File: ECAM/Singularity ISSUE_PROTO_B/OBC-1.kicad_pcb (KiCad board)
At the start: 6 copper layers, 42.8 x 42.8 mm, 111 parts, among them J1 ERM8-020-X, J2 ERF6-020-X, J3 Conn_01x02_Female, Q1 MGSF1N02L, Q2 MGSF1N02L, U1 TPS62850x-Q1, U10 FM33256B, U11 TMS5701227CZWTQQ1, U2 TPS62850x-Q1, U3 LTC4353, U4 SN65HVD230M-EP, U5 SN65HVD230M-EP, U6 SN65HVD230M-EP, U7 CY15B108QI, U8 S70FL01GS, X1 ASTMTXK-32.768KHZ, X2 LFTCXO075797

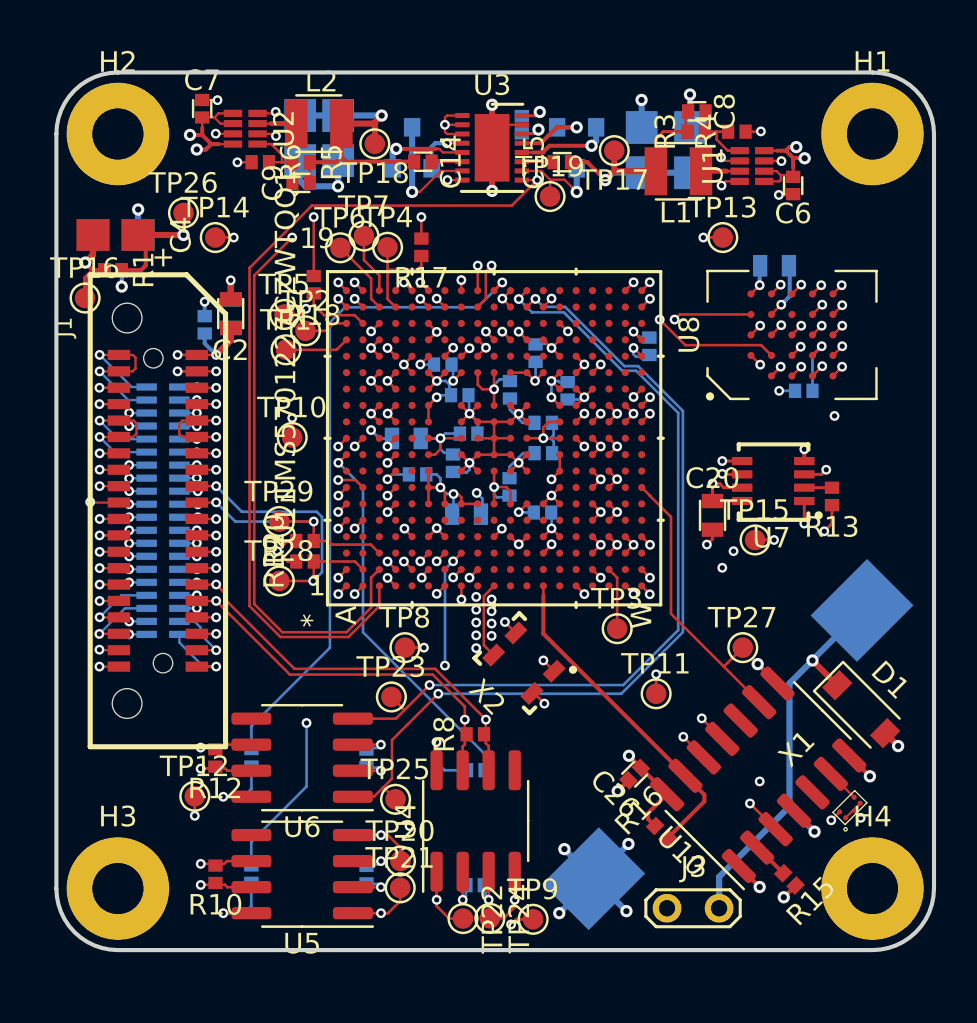
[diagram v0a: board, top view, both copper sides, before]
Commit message: updated PCB layout for Issue B supervisor/RTC circuitry
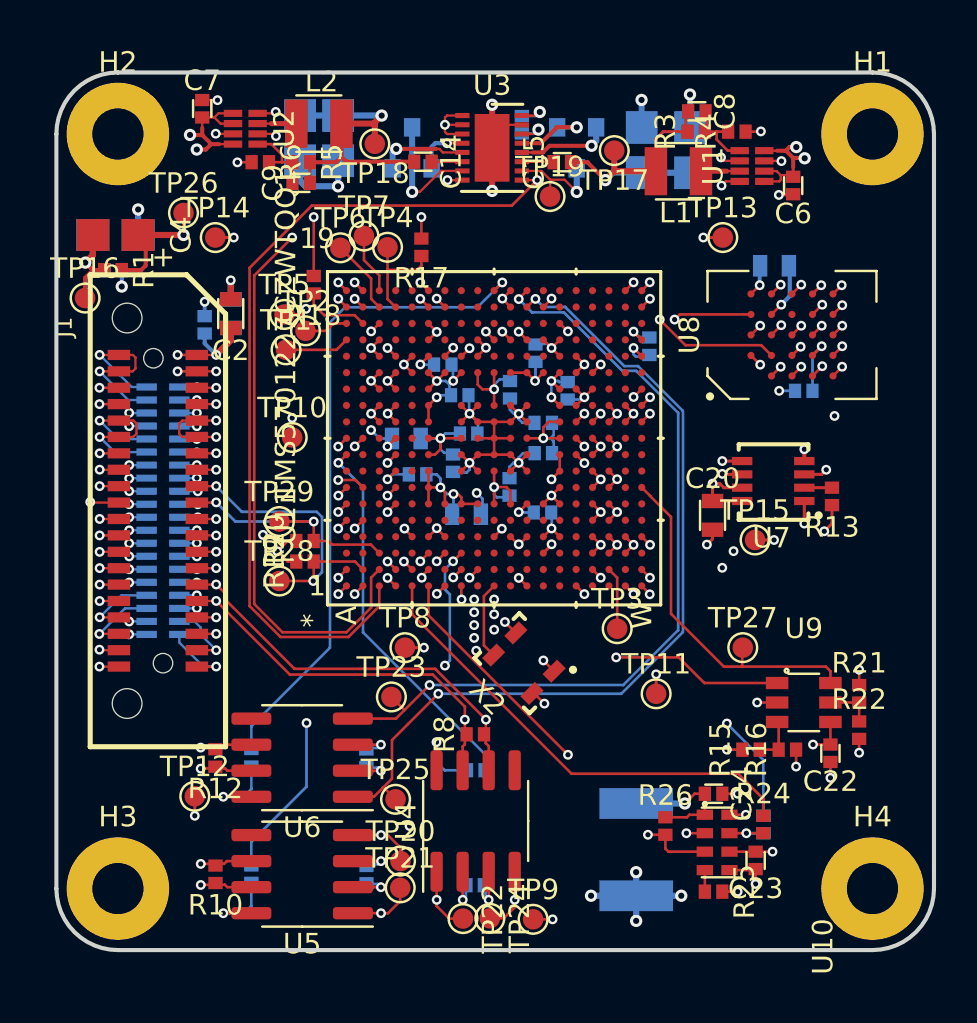
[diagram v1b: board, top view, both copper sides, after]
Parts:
- removed C26: 100n-10V-0402-5%-CER, TFT_C_passive_SMD:0402_CAP
- removed C27: 4F-2V8-14x7mm_supercap, TFT_C_passive_SMD:MAL219691152E3_short
- removed D1: MMSZ5223BT1G, Diode_SMD:D_SOD-123
- removed J3: Conn_01x02_Female, TFT_TestPoints:TP_2Pads_Pitch2.54mm_Drill0.8mm
- removed X1: ASTMTXK-32.768KHZ, TFT_BGA:ASTMTXK_OSC
- added C22: 100n-10V-0402-5%-CER, TFT_C_passive_SMD:0402_CAP, F.Cu at (126.7, 104.7)
- added C23: 100n-10V-0402-5%-CER, TFT_C_passive_SMD:0402_CAP, F.Cu at (123.0, 109.9)
- added C24: 100n-10V-0402-5%-CER, TFT_C_passive_SMD:0402_CAP, F.Cu at (120.9, 106.7)
- added C25: 100uAH-1V8-4.4x3mm_LIon_batt, TFT_misc:1812_BATT, B.Cu at (117.2, 109.4)
- added R21: 0R-50V-0402, TFT_R_passive_SMD:0402_RES, F.Cu at (128.1, 101.8)
- added R22: 0R-50V-0402, TFT_R_passive_SMD:0402_RES, F.Cu at (128.1, 103.6)
- added R23: 0R-50V-0402, TFT_R_passive_SMD:0402_RES, B.Cu at (123.4, 108.2)
- added R24: 0R-50V-0402, TFT_R_passive_SMD:0402_RES, F.Cu at (123.4, 108.2)
- added R25: 10K-50V-0402-1%, TFT_R_passive_SMD:0402_RES, F.Cu at (121.0, 111.5)
- added R26: 10K-50V-0402-1%, TFT_R_passive_SMD:0402_RES, F.Cu at (118.6, 108.2)
- added U9: TPS3813K33-EP, TFT_SOT:SOT-236, F.Cu at (125.3, 102.2)
- R15: value 39R0-50V-0402-1% -> 0R-50V-0402
- R16: value 4K7-50V-0402-1% -> 0R-50V-0402
- U10: value FM33256B -> RV-3032-C7; footprint Package_SO:SOIC-14_3.9x8.7mm_P1.27mm -> TFT_misc:RV-3032-C7
- moved R16 7.35 mm to (124.5, 104.5), turned to 90 degrees
- moved R15 6.60 mm to (122.8, 104.5), turned to 90 degrees
- moved U10 3.86 mm to (121.1, 109.0), turned to 270 degrees
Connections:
- J1 pad 10: /TMS570_uC/OBC_I2C_SCL -> /RTC/OBC_I2C_SCL
- J1 pad 9: /TMS570_uC/OBC_I2C_SDA -> /RTC/OBC_I2C_SDA
- R15 pad 1: /Supervisor_RTC_FRAM/SPVSR_CIPO -> OBC_3V3
- R15 pad 2: Net-(R15-Pad2) -> /Supervisor/WDT
- R16 pad 1: OBC_3V3 -> /Supervisor/WDT
- R16 pad 2: /Supervisor_RTC_FRAM/SPVSR_ACS -> GND
- R19 pad 2: /TMS570_uC/OBC_I2C_SDA -> /RTC/OBC_I2C_SDA
- R20 pad 2: /TMS570_uC/OBC_I2C_SCL -> /RTC/OBC_I2C_SCL
- TP27 pad 1: /Supervisor_RTC_FRAM/SPVSR_nRST -> /Supervisor/SPVSR_nRST
- TP28 pad 1: /TMS570_uC/OBC_I2C_SDA -> /RTC/OBC_I2C_SDA
- TP29 pad 1: /TMS570_uC/OBC_I2C_SCL -> /RTC/OBC_I2C_SCL
- U10 pad 1: /Supervisor_RTC_FRAM/SPVSR_nCS -> OBC_RTC_Vbackup
- U10 pad 2: Net-(R15-Pad2) -> /RTC/OBC_I2C_SDA
- U10 pad 3: /Supervisor_RTC_FRAM/SPVSR_CNT -> /RTC/RTC_nINT
- U10 pad 4: OBC_RTC_Vbackup -> Net-(R25-Pad2)
- U10 pad 5: Net-(U10-Pad5) -> GND
- U10 pad 6: Net-(U10-Pad6) -> OBC_3V3
- U10 pad 7: GND -> /RTC/RTC_CLKOUT
- U10 pad 8: GND -> /RTC/OBC_I2C_SCL
- U11 pad B2: /TMS570_uC/OBC_I2C_SDA -> /RTC/OBC_I2C_SDA
- U11 pad C3: /TMS570_uC/OBC_I2C_SCL -> /RTC/OBC_I2C_SCL
- U11 pad E19: /Supervisor_RTC_FRAM/SPVSR_nCS -> Net-(U11-PadE19)
- U11 pad F1: Net-(U11-PadF1) -> /RTC/RTC_nINT
- U11 pad H19: /Supervisor_RTC_FRAM/SPVSR_CLK -> Net-(U11-PadH19)
- U11 pad J18: /Supervisor_RTC_FRAM/SPVSR_CIPO -> Net-(U11-PadJ18)
- U11 pad J19: /Supervisor_RTC_FRAM/SPVSR_COPI -> Net-(U11-PadJ19)
- U11 pad J2: /Supervisor_RTC_FRAM/SPVSR_CNT -> /Supervisor/SPVSR_PET
- U11 pad M1: Net-(U11-PadM1) -> /Connectors/ADS_nRST
- U11 pad N1: /Supervisor_RTC_FRAM/SPVSR_ACS -> Net-(U11-PadN1)
- U11 pad W7: /Supervisor_RTC_FRAM/SPVSR_nRST -> /Supervisor/SPVSR_nRST
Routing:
- net /RTC/OBC_I2C_SCL: track 0.00 -> 54.0 mm, vias 0 -> 3
- net /RTC/OBC_I2C_SDA: track 0.00 -> 51.4 mm, vias 0 -> 3
- net /Supervisor_RTC_FRAM/SPVSR_nCS: track 48.3 -> 0.00 mm, vias 3 -> 0
- net /Supervisor_RTC_FRAM/SPVSR_CIPO: track 44.8 -> 0.00 mm, vias 2 -> 0
- net /Supervisor_RTC_FRAM/SPVSR_COPI: track 35.2 -> 0.00 mm, vias 2 -> 0
- net /Supervisor_RTC_FRAM/SPVSR_CLK: track 35.0 -> 0.00 mm, vias 2 -> 0
- net Net-(R24-Pad1): track 0.00 -> 23.1 mm
- net Net-(R23-Pad1): track 0.00 -> 21.4 mm, vias 0 -> 2
- net /Supervisor_RTC_FRAM/SPVSR_CNT: track 20.6 -> 0.00 mm, vias 2 -> 0
- net /RTC/RTC_nINT: track 0.00 -> 20.1 mm, vias 0 -> 2
- net /Supervisor/SPVSR_PET: track 0.00 -> 17.7 mm, vias 0 -> 2
- net /Supervisor/SPVSR_nRST: track 0.00 -> 17.2 mm
- net /Connectors/ADS_nRST: track 0.95 -> 17.4 mm, vias 1 -> 3
- net /Supervisor_RTC_FRAM/SPVSR_ACS: track 16.3 -> 0.00 mm
- net OBC_RTC_Vbackup: track 22.3 -> 6.55 mm, vias 2 -> 1
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
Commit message: file cleanup
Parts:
- moved TP9 4.29 mm to (113.4, 108.7)
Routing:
- net /FL_1/FL_1_SI_IO0: track 23.5 -> 22.1 mm
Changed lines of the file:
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@@
     (thickness 1.6)
     (drawings 8)
-    (tracks 1772)
+    (tracks 1768)
     (zones 0)
     (modules 117)
@@
   )
   (module TFT_TestPoints:TP_RDPad_D1.0mm (layer F.Cu)
-    (at 112.15 112.8)
+    (at 113.425 108.7)
     (descr "SMD pad as test Point, diameter 1.0mm")
     (tags "test point SMD pad")
@@
   (via (at 122.125 106.675) (size 0.48) (drill 0.25) (layers F.Cu B.Cu) (net 2))
   (segment (start 121.375 106.675) (end 122.125 106.675) (width 0.13) (layer F.Cu) (net 2))
-  (via (at 113.1 112.8) (size 0.48) (drill 0.25) (layers F.Cu B.Cu) (net 2))
-  (segment (start 112.15 112.8) (end 113.1 112.8) (width 0.13) (layer F.Cu) (net 2))
+  (via (at 114.375 108.7) (size 0.48) (drill 0.25) (layers F.Cu B.Cu) (net 2))
+  (segment (start 113.425 108.7) (end 114.375 108.7) (width 0.13) (layer F.Cu) (net 2))
   (segment (start 117.175 111.65) (end 117.175 110.5) (width 0.3) (layer B.Cu) (net 2))
   (via (at 117.175 110.5) (size 0.6) (drill 0.3) (layers F.Cu B.Cu) (net 2))
@@
   (segment (start 107.448169 82.538689) (end 107.448169 82.527468) (width 0.13) (layer F.Cu) (net 30))
   (segment (start 107.84792 82.93844) (end 107.448169 82.538689) (width 0.13) (layer F.Cu) (net 30))
-  (segment (start 123.810589 87.025) (end 124.15 87.025) (width 0.13) (layer In3.Cu) (net 30))
-  (segment (start 119.74059 82.955001) (end 123.810589 87.025) (width 0.13) (layer In3.Cu) (net 30))
-  (segment (start 107.875702 82.955001) (end 119.74059 82.955001) (width 0.13) (layer In3.Cu) (net 30))
+  (segment (start 123.55 87.025) (end 124.15 87.025) (width 0.13) (layer In3.Cu) (net 30))
+  (segment (start 119.480001 82.955001) (end 123.55 87.025) (width 0.13) (layer In3.Cu) (net 30))
+  (segment (start 107.875702 82.955001) (end 119.480001 82.955001) (width 0.13) (layer In3.Cu) (net 30))
   (segment (start 107.448169 82.527468) (end 107.875702 82.955001) (width 0.13) (layer In3.Cu) (net 30))
   (segment (start 112.64792 96.538439) (end 112.648895 96.538439) (width 0.13) (layer F.Cu) (net 221))
@@
   (segment (start 107.046952 82.138441) (end 106.648092 81.739581) (width 0.13) (layer F.Cu) (net 120))
   (segment (start 107.04792 82.13844) (end 107.046952 82.138441) (width 0.13) (layer F.Cu) (net 120))
-  (segment (start 125.675 83.3) (end 122.025 83.3) (width 0.13) (layer In3.Cu) (net 120))
-  (segment (start 118.225 79.5) (end 108.887673 79.5) (width 0.13) (layer In3.Cu) (net 120))
-  (segment (start 126.225 83.85) (end 125.675 83.3) (width 0.13) (layer In3.Cu) (net 120))
-  (segment (start 108.887673 79.5) (end 106.648092 81.739581) (width 0.13) (layer In3.Cu) (net 120))
-  (segment (start 122.025 83.3) (end 118.225 79.5) (width 0.13) (layer In3.Cu) (net 120))
   (via (at 126.225 83.85) (size 0.48) (drill 0.25) (layers F.Cu B.Cu) (net 120))
   (segment (start 125.775 84.3) (end 126.225 83.85) (width 0.13) (layer F.Cu) (net 120))
+  (segment (start 107.187673 81.2) (end 106.648092 81.739581) (width 0.13) (layer In3.Cu) (net 120))
+  (segment (start 119.925 81.2) (end 107.187673 81.2) (width 0.13) (layer In3.Cu) (net 120))
+  (segment (start 122.025 83.3) (end 119.925 81.2) (width 0.13) (layer In3.Cu) (net 120))
+  (segment (start 125.675 83.3) (end 122.025 83.3) (width 0.13) (layer In3.Cu) (net 120))
+  (segment (start 126.225 83.85) (end 125.675 83.3) (width 0.13) (layer In3.Cu) (net 120))
   (segment (start 107.04792 82.937472) (end 106.64792 82.537473) (width 0.13) (layer F.Cu) (net 121))
   (via (at 106.64792 82.537473) (size 0.48) (drill 0.25) (layers F.Cu B.Cu) (net 121))
@@
   (via (at 122.525 107.7) (size 0.48) (drill 0.25) (layers F.Cu B.Cu) (net 206))
   (segment (start 121.725 107.7) (end 122.525 107.7) (width 0.13) (layer F.Cu) (net 206))
-  (segment (start 122.525 107.7) (end 119.625 107.7) (width 0.13) (layer In3.Cu) (net 206))
+  (segment (start 119.625 107.7) (end 122.525 107.7) (width 0.13) (layer In3.Cu) (net 206))
+  (segment (start 114.371099 109.353901) (end 117.971099 109.353901) (width 0.13) (layer In3.Cu) (net 206))
+  (segment (start 104.406681 112.906681) (end 110.818319 112.906681) (width 0.13) (layer In3.Cu) (net 206))
   (segment (start 102.243039 110.743039) (end 104.406681 112.906681) (width 0.13) (layer In3.Cu) (net 206))
-  (segment (start 119.625 107.7) (end 117.971099 109.353901) (width 0.13) (layer In3.Cu) (net 206))
-  (segment (start 105.243319 112.906681) (end 105.896099 112.253901) (width 0.13) (layer In3.Cu) (net 206))
-  (segment (start 104.406681 112.906681) (end 105.243319 112.906681) (width 0.13) (layer In3.Cu) (net 206))
-  (segment (start 102.25 94.2) (end 102.243039 94.206961) (width 0.13) (layer In3.Cu) (net 206))
   (segment (start 102.243039 94.206961) (end 102.243039 110.743039) (width 0.13) (layer In3.Cu) (net 206))
+  (segment (start 110.818319 112.906681) (end 114.371099 109.353901) (width 0.13) (layer In3.Cu) (net 206))
+  (segment (start 102.25 94.2) (end 102.243039 94.206961) (width 0.13) (layer In3.Cu) (net 206))
+  (segment (start 117.971099 109.353901) (end 119.625 107.7) (width 0.13) (layer In3.Cu) (net 206))
   (segment (start 101.45 93.4) (end 102.25 94.2) (width 0.13) (layer In3.Cu) (net 206))
-  (segment (start 117.971099 109.353901) (end 114.371099 109.353901) (width 0.13) (layer In3.Cu) (net 206))
-  (segment (start 111.471099 112.253901) (end 105.896099 112.253901) (width 0.13) (layer In3.Cu) (net 206))
-  (segment (start 114.371099 109.353901) (end 111.471099 112.253901) (width 0.13) (layer In3.Cu) (net 206))
   (via (at 119.625 108.6) (size 0.48) (drill 0.25) (layers F.Cu B.Cu) (net 207))
   (segment (start 120.525 108.6) (end 119.625 108.6) (width 0.13) (layer F.Cu) (net 207))
@@
   (segment (start 102 110.875) (end 102 96.875) (width 0.13) (layer In3.Cu) (net 207))
   (segment (start 104.261691 113.136691) (end 102 110.875) (width 0.13) (layer In3.Cu) (net 207))
-  (segment (start 105.338592 113.136691) (end 104.261691 113.136691) (width 0.13) (layer In3.Cu) (net 207))
-  (segment (start 105.975282 112.5) (end 105.338592 113.136691) (width 0.13) (layer In3.Cu) (net 207))
-  (segment (start 114.458186 109.592096) (end 111.550282 112.5) (width 0.13) (layer In3.Cu) (net 207))
+  (segment (start 110.913591 113.136691) (end 104.261691 113.136691) (width 0.13) (layer In3.Cu) (net 207))
+  (segment (start 114.458186 109.592096) (end 110.913591 113.136691) (width 0.13) (layer In3.Cu) (net 207))
   (segment (start 118.632904 109.592096) (end 114.458186 109.592096) (width 0.13) (layer In3.Cu) (net 207))
-  (segment (start 111.550282 112.5) (end 105.975282 112.5) (width 0.13) (layer In3.Cu) (net 207))
   (segment (start 119.625 108.6) (end 118.632904 109.592096) (width 0.13) (layer In3.Cu) (net 207))
   (segment (start 124.125 104.525) (end 123.2 104.525) (width 0.13) (layer F.Cu) (net 208))
@@
         (xy 99.9 103.75) (xy 105.4 103.725) (xy 105.4 105.025) (xy 99.9 105.05) (xy 99.9 106.8)
         (xy 102.4 109.55) (xy 109.9 109.55) (xy 114.575 105.025) (xy 114.57618 104.773843) (xy 112.05 102.2)
-        (xy 112.575 101.675) (xy 115.425 104.425) (xy 117.4 104.4) (xy 117.4 105.3) (xy 115.45 105.3)
+        (xy 112.575 101.675) (xy 115.625 104.6) (xy 117.4 104.6) (xy 117.4 105.1) (xy 115.675 105.1)
         (xy 110.65 110) (xy 110.65 112.3) (xy 109.15 112.3) (xy 109.15 110.55) (xy 101.9 110.55)
         (xy 98.9 107.3) (xy 98.9 103.8) (xy 97.15 102.05) (xy 97.15 86.55) (xy 94.15 86.55)
